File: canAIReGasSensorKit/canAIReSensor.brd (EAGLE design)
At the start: 50.8 x 31.8 mm, 19 parts, among them IC1 LP2951N, IC2 AD820N, Q1 FQN1N50CI, Q2 FQN1N50CI, X1 SSW-102-02-S-D

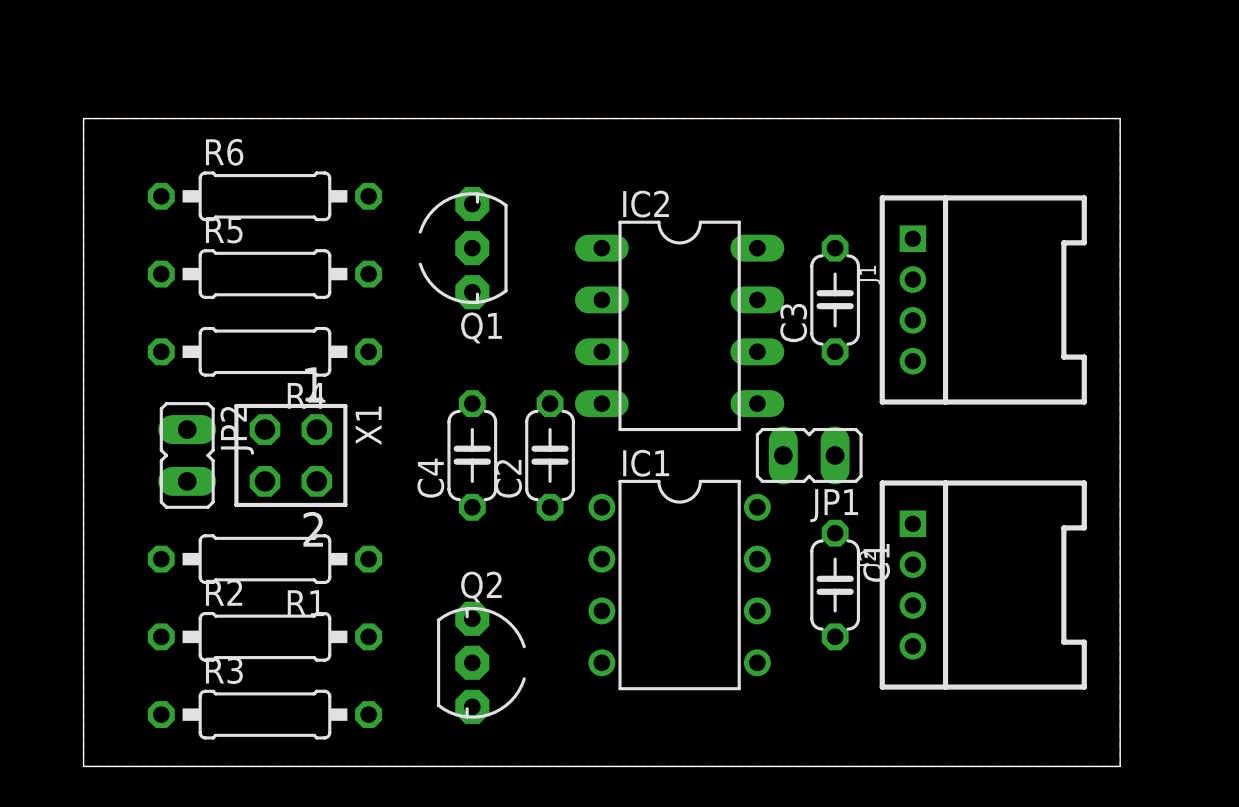
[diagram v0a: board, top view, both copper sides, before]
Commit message: initial routing compleated
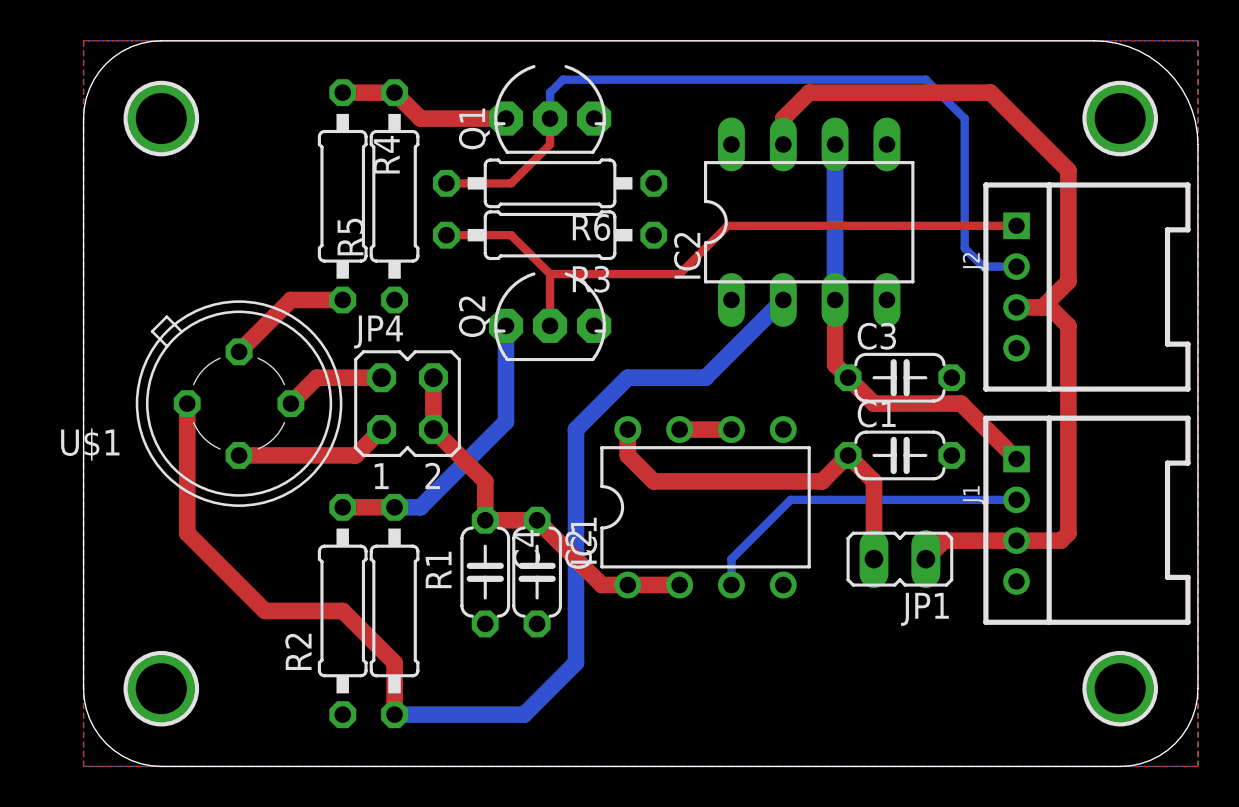
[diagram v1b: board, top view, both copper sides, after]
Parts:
- removed JP2: (no value), jumper:JP1
- removed X1: SSW-102-02-S-D, con-samtec:SSW-102-02-S-D
- added JP4: (no value), jumper:JP2Q
- added U$1: E2V_MICS, open_hw_sockets:E2V_MICS
- added U$2, U$3, U$4, U$5: MOUNTINGHOLE2.5, microbuilder:MOUNTINGHOLE_2.5_PLATED
- moved R3 27.3 mm to (22.9, 26.0), turned to 180 degrees
- moved Q2 16.9 mm to (22.9, 21.6), turned to 0 degrees
- moved J2 15.5 mm to (45.7, 23.5)
- moved R6 14.0 mm to (22.9, 28.6), turned to 180 degrees
- moved J1 11.9 mm to (45.7, 12.1)
- moved R4 8.52 mm to (12.7, 27.9), turned to 270 degrees
- moved IC2 8.13 mm to (35.6, 26.7), turned to 0 degrees
- moved R5 7.41 mm to (15.2, 27.9), turned to 90 degrees
- moved Q1 7.41 mm to (22.9, 31.8), turned to 0 degrees
- moved C1 7.10 mm to (40.0, 15.2), turned to 0 degrees
- moved R1 6.84 mm to (15.2, 7.62), turned to 270 degrees
- moved JP1 6.75 mm to (40.0, 10.2)
- moved C2 5.75 mm to (22.2, 9.53), turned to 270 degrees
- moved C4 5.75 mm to (19.7, 9.53), turned to 270 degrees
- moved C3 4.96 mm to (40.0, 19.1), turned to 0 degrees
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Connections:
- removed net S0: IC2.2, R1.2, X1.2
- removed net VIN: IC1.8, JP1.2
- new net N$3: JP4.1, U$1.3
- new net N$5: C1.1, IC1.8, JP1.2
- new net S2: IC2.2, R1.2, U$1.2
- net HPWR: now also JP4.2, JP4.4; no longer JP2.1, X1.3
- net N$2: now also U$1.1; no longer X1.1
- net S1: now also JP4.3, U$1.4; no longer JP2.2, X1.4
- net VCC: now also IC2.7; no longer C1.1
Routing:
- net S2: track 0.00 -> 55.8 mm
- net VCC: track 0.00 -> 45.2 mm
- net OVERHEAT: track 0.00 -> 39.0 mm
- net RANGE: track 0.00 -> 32.2 mm
- net SENSOR: track 0.00 -> 21.6 mm
- net HPWR: track 0.00 -> 18.9 mm
- net N$5: track 0.00 -> 18.7 mm
- net HEATER: track 0.00 -> 16.4 mm
- net N$1: track 0.00 -> 14.4 mm
- net N$6: track 0.00 -> 8.53 mm
- net N$3: track 0.00 -> 7.51 mm
- net N$2: track 0.00 -> 6.13 mm
- net S1: track 0.00 -> 4.97 mm
- net N$4: track 0.00 -> 2.54 mm
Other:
- board size 50.8 x 31.8 mm -> 54.6 x 35.6 mm
